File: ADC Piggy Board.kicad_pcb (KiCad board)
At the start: 2 copper layers, 50 x 89.2 mm, 7 parts, among them J1 ADC J4, J3 ADC J14, J4 ADC J15, J6 Power, J7 FPGA

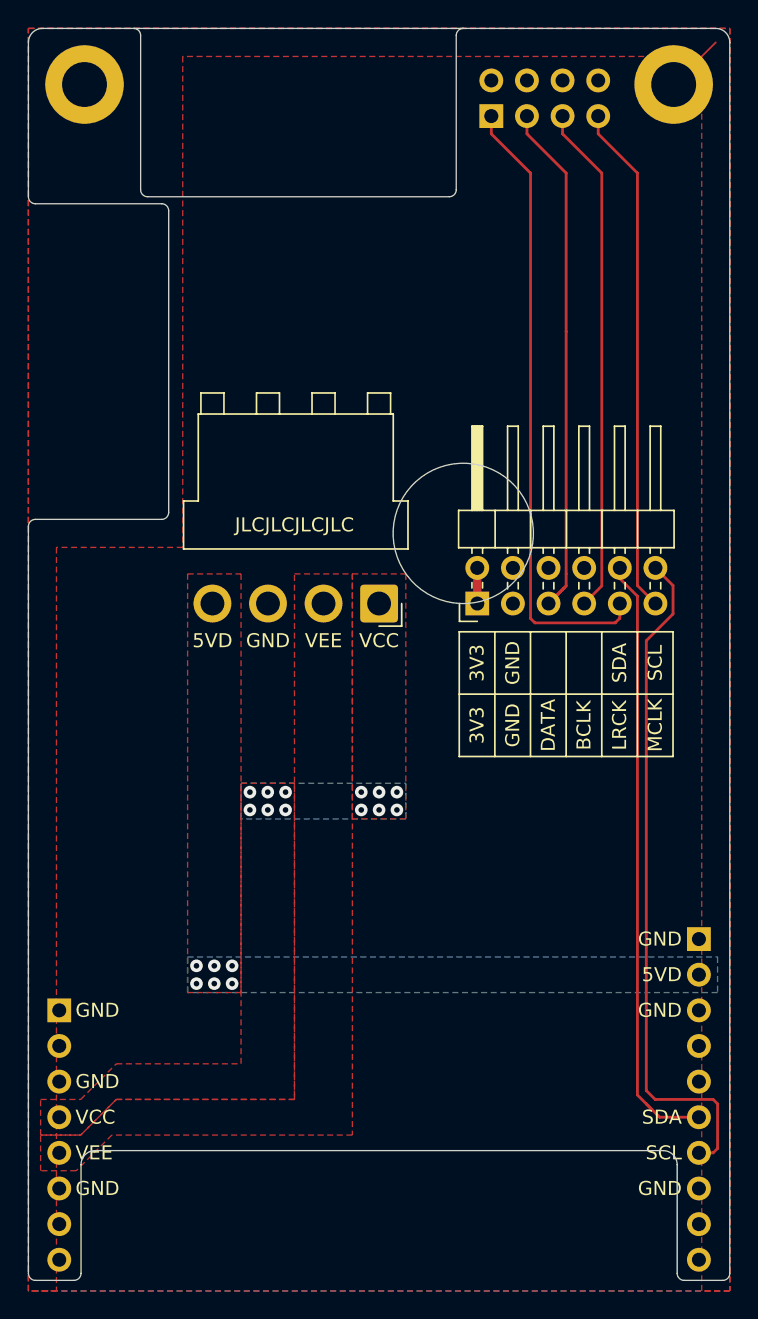
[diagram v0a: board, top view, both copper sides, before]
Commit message: Update to KiCad 6
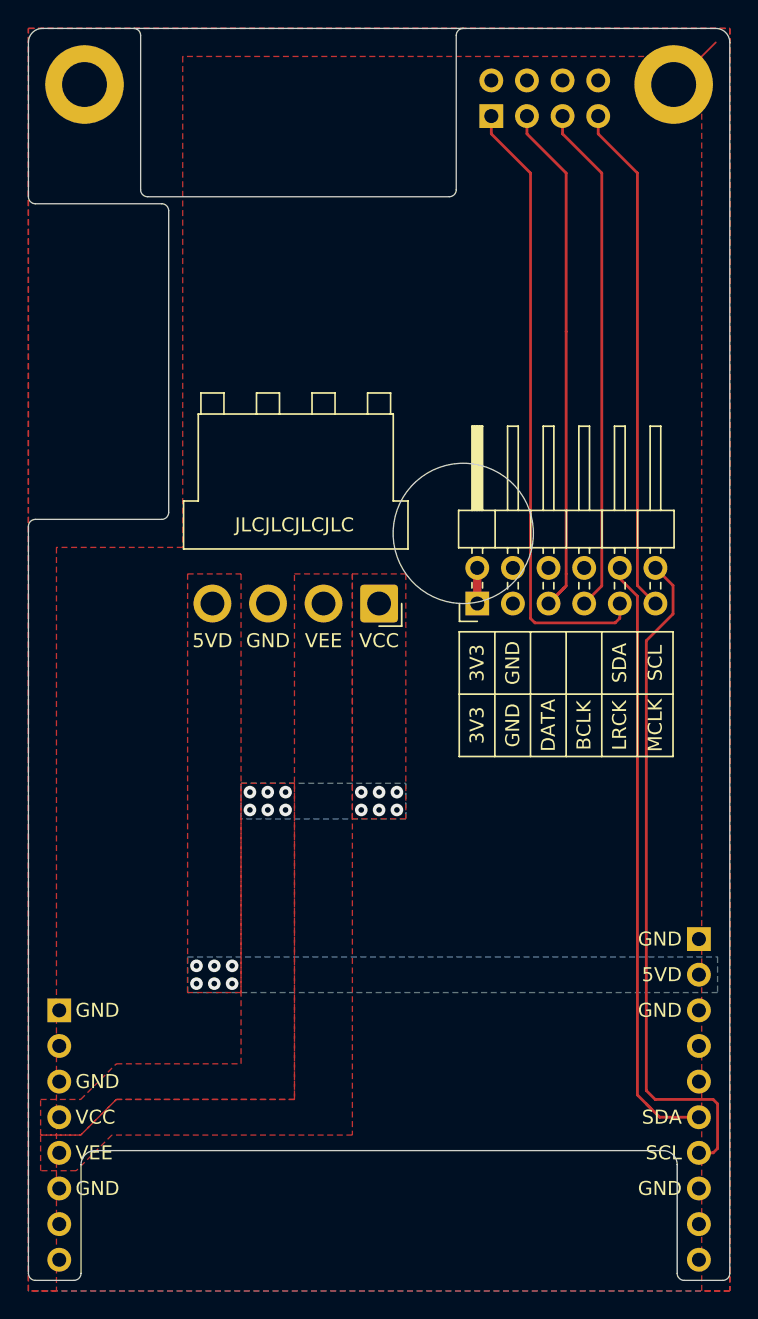
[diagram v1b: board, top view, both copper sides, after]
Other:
- net class Default removed
